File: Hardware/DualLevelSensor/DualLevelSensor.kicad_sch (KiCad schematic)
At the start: 95 parts, among them J1 USB_B_Micro, J2 Conn_01x03, J3 Conn_01x03, J4 Conn_01x03, J5 Conn_01x02, K1 capPad, K10 capPad, K11 capPad, K12 capPad, K13 capPad, K14 capPad, K15 capPad, K16 capPad, K17 capPad, K18 capPad, K19 capPad, K2 capPad, K20 capPad, K21 capPad, K22 capPad, K3 capPad, K4 capPad, K5 capPad, K6 capPad, K7 capPad, K8 capPad, K9 capPad, U1 W25Q16JVUXIQ, U2 RP2040, U3 AP63357Q, Y1 12Mhz

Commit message: Bugfixes
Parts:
- C4, C5: value 100n -> 10n
- R5, R6: value 1k -> 100R
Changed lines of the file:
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@@
   (symbol (lib_id "Device:R") (at 111.76 44.45 270) (unit 1)
     (in_bom yes) (on_board yes)
-    (property "Reference" "R5" (id 0) (at 106.68 43.18 90)
-      (effects (font (size 1.27 1.27)) (justify right))
-    )
-    (property "Value" "1k" (id 1) (at 113.03 44.45 90)
+    (property "Reference" "R5" (id 0) (at 107.95 43.18 90)
+      (effects (font (size 1.27 1.27)) (justify right))
+    )
+    (property "Value" "100R" (id 1) (at 114.3 44.45 90)
       (effects (font (size 1.27 1.27)) (justify right))
     )
@@
       (effects (font (size 1.27 1.27)) (justify right))
     )
-    (property "Value" "100n" (id 1) (at 123.19 40.64 0)
+    (property "Value" "10n" (id 1) (at 123.19 40.64 0)
       (effects (font (size 1.27 1.27)) (justify right))
     )
@@
       (effects (font (size 1.27 1.27)) (justify right))
     )
-    (property "Value" "100n" (id 1) (at 132.08 40.64 0)
+    (property "Value" "10n" (id 1) (at 132.08 40.64 0)
       (effects (font (size 1.27 1.27)) (justify right))
     )
@@
   (symbol (lib_id "Device:R") (at 111.76 46.99 270) (unit 1)
     (in_bom yes) (on_board yes)
-    (property "Reference" "R6" (id 0) (at 106.68 45.72 90)
-      (effects (font (size 1.27 1.27)) (justify right))
-    )
-    (property "Value" "1k" (id 1) (at 113.03 46.99 90)
+    (property "Reference" "R6" (id 0) (at 107.95 45.72 90)
+      (effects (font (size 1.27 1.27)) (justify right))
+    )
+    (property "Value" "100R" (id 1) (at 114.3 46.99 90)
       (effects (font (size 1.27 1.27)) (justify right))
     )
@@
     )
     (path "/65943053-8f32-46c6-b519-686508c88415"
-      (reference "C4") (unit 1) (value "100n") (footprint "Capacitor_SMD:C_0603_1608Metric")
+      (reference "C4") (unit 1) (value "10n") (footprint "Capacitor_SMD:C_0603_1608Metric")
     )
     (path "/7dc2a189-f59a-4e30-9c4f-94db9b59d31d"
-      (reference "C5") (unit 1) (value "100n") (footprint "Capacitor_SMD:C_0603_1608Metric")
+      (reference "C5") (unit 1) (value "10n") (footprint "Capacitor_SMD:C_0603_1608Metric")
     )
     (path "/f29801a0-5499-4f14-9b3f-f02bc31c5830"
@@
     )
     (path "/6484fdb6-b4a3-470a-a334-696f73f9da81"
-      (reference "R5") (unit 1) (value "1k") (footprint "Resistor_SMD:R_0603_1608Metric")
+      (reference "R5") (unit 1) (value "100R") (footprint "Resistor_SMD:R_0603_1608Metric")
     )
     (path "/9e9bfdb2-da9b-4608-a601-767cea21e58b"
-      (reference "R6") (unit 1) (value "1k") (footprint "Resistor_SMD:R_0603_1608Metric")
+      (reference "R6") (unit 1) (value "100R") (footprint "Resistor_SMD:R_0603_1608Metric")
     )
     (path "/e23417b8-354a-431a-a64a-3bb72eb32e4b"

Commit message: values corrected
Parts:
- L2: value 1µ -> 10µ
- R33, R34: value 1k -> 100R
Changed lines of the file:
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@@
     (in_bom yes) (on_board yes) (fields_autoplaced)
     (property "Reference" "L2" (id 0) (at 168.91 26.67 90))
-    (property "Value" "1µ" (id 1) (at 168.91 29.21 90))
+    (property "Value" "10µ" (id 1) (at 168.91 29.21 90))
     (property "Footprint" "Inductor_SMD:L_0805_2012Metric" (id 2) (at 168.91 31.75 0)
       (effects (font (size 1.27 1.27)) hide)
@@
       (effects (font (size 1.27 1.27)) (justify right))
     )
-    (property "Value" "1k" (id 1) (at 154.94 144.78 90)
+    (property "Value" "100R" (id 1) (at 156.21 144.78 90)
       (effects (font (size 1.27 1.27)) (justify right))
     )
@@
       (effects (font (size 1.27 1.27)) (justify right))
     )
-    (property "Value" "1k" (id 1) (at 154.94 154.94 90)
+    (property "Value" "100R" (id 1) (at 156.21 154.94 90)
       (effects (font (size 1.27 1.27)) (justify right))
     )
@@
     )
     (path "/21efa11b-39d3-4f53-ba2c-acb613f9de54"
-      (reference "L2") (unit 1) (value "1µ") (footprint "Inductor_SMD:L_0805_2012Metric")
+      (reference "L2") (unit 1) (value "10µ") (footprint "Inductor_SMD:L_0805_2012Metric")
     )
     (path "/e24d31a3-fcfc-40dd-92eb-52ff5fe4874c"
@@
     )
     (path "/669d3c1d-b951-41bd-a3a2-fed461816925"
-      (reference "R33") (unit 1) (value "1k") (footprint "Resistor_SMD:R_0603_1608Metric")
+      (reference "R33") (unit 1) (value "100R") (footprint "Resistor_SMD:R_0603_1608Metric")
     )
     (path "/694bc754-7a9d-4f76-9f8b-5a052602e308"
-      (reference "R34") (unit 1) (value "1k") (footprint "Resistor_SMD:R_0603_1608Metric")
+      (reference "R34") (unit 1) (value "100R") (footprint "Resistor_SMD:R_0603_1608Metric")
     )
     (path "/0399bf47-770b-4c30-8650-a3df6edc8cf3"

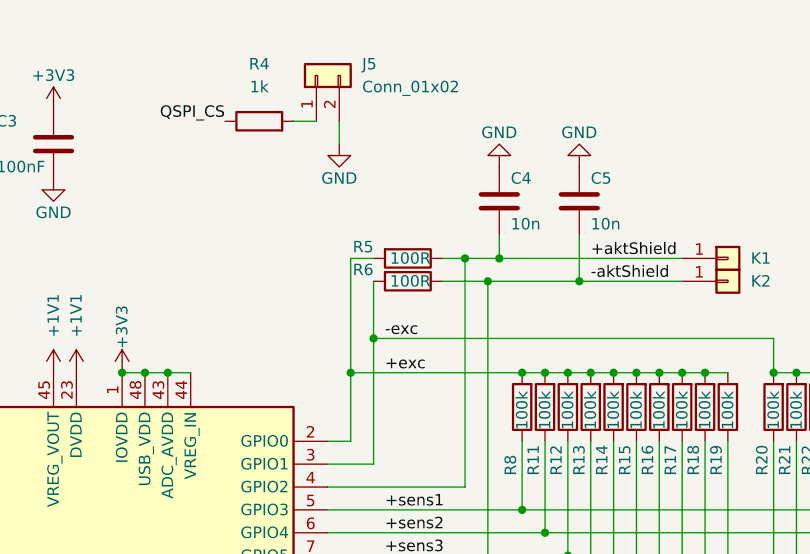
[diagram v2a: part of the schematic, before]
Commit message: capLevelSens seams to Work
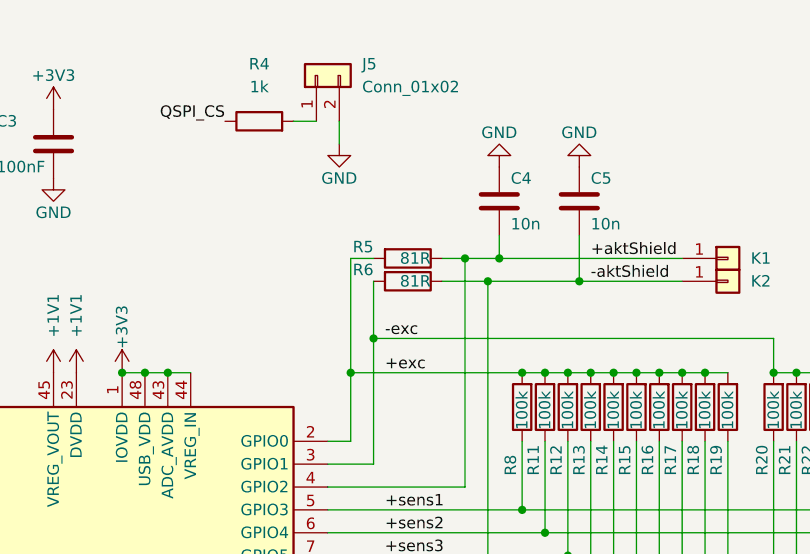
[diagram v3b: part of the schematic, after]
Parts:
- R5, R6: value 100R -> 81R
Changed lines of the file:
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@@
       (effects (font (size 1.27 1.27)) (justify right))
     )
-    (property "Value" "100R" (id 1) (at 114.3 44.45 90)
+    (property "Value" "81R" (id 1) (at 114.3 44.45 90)
       (effects (font (size 1.27 1.27)) (justify right))
     )
@@
       (effects (font (size 1.27 1.27)) (justify right))
     )
-    (property "Value" "100R" (id 1) (at 114.3 46.99 90)
+    (property "Value" "81R" (id 1) (at 114.3 46.99 90)
       (effects (font (size 1.27 1.27)) (justify right))
     )
@@
     )
     (path "/6484fdb6-b4a3-470a-a334-696f73f9da81"
-      (reference "R5") (unit 1) (value "100R") (footprint "Resistor_SMD:R_0603_1608Metric")
+      (reference "R5") (unit 1) (value "81R") (footprint "Resistor_SMD:R_0603_1608Metric")
     )
     (path "/9e9bfdb2-da9b-4608-a601-767cea21e58b"
-      (reference "R6") (unit 1) (value "100R") (footprint "Resistor_SMD:R_0603_1608Metric")
+      (reference "R6") (unit 1) (value "81R") (footprint "Resistor_SMD:R_0603_1608Metric")
     )
     (path "/e23417b8-354a-431a-a64a-3bb72eb32e4b"
